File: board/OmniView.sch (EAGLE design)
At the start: 50 parts, among them Q1 CMA-4544PF-W, Q2 BSS138, Q3 BSS138, U1 SN74LVC2T45DCUT, U2 UG-2864HSWEG01

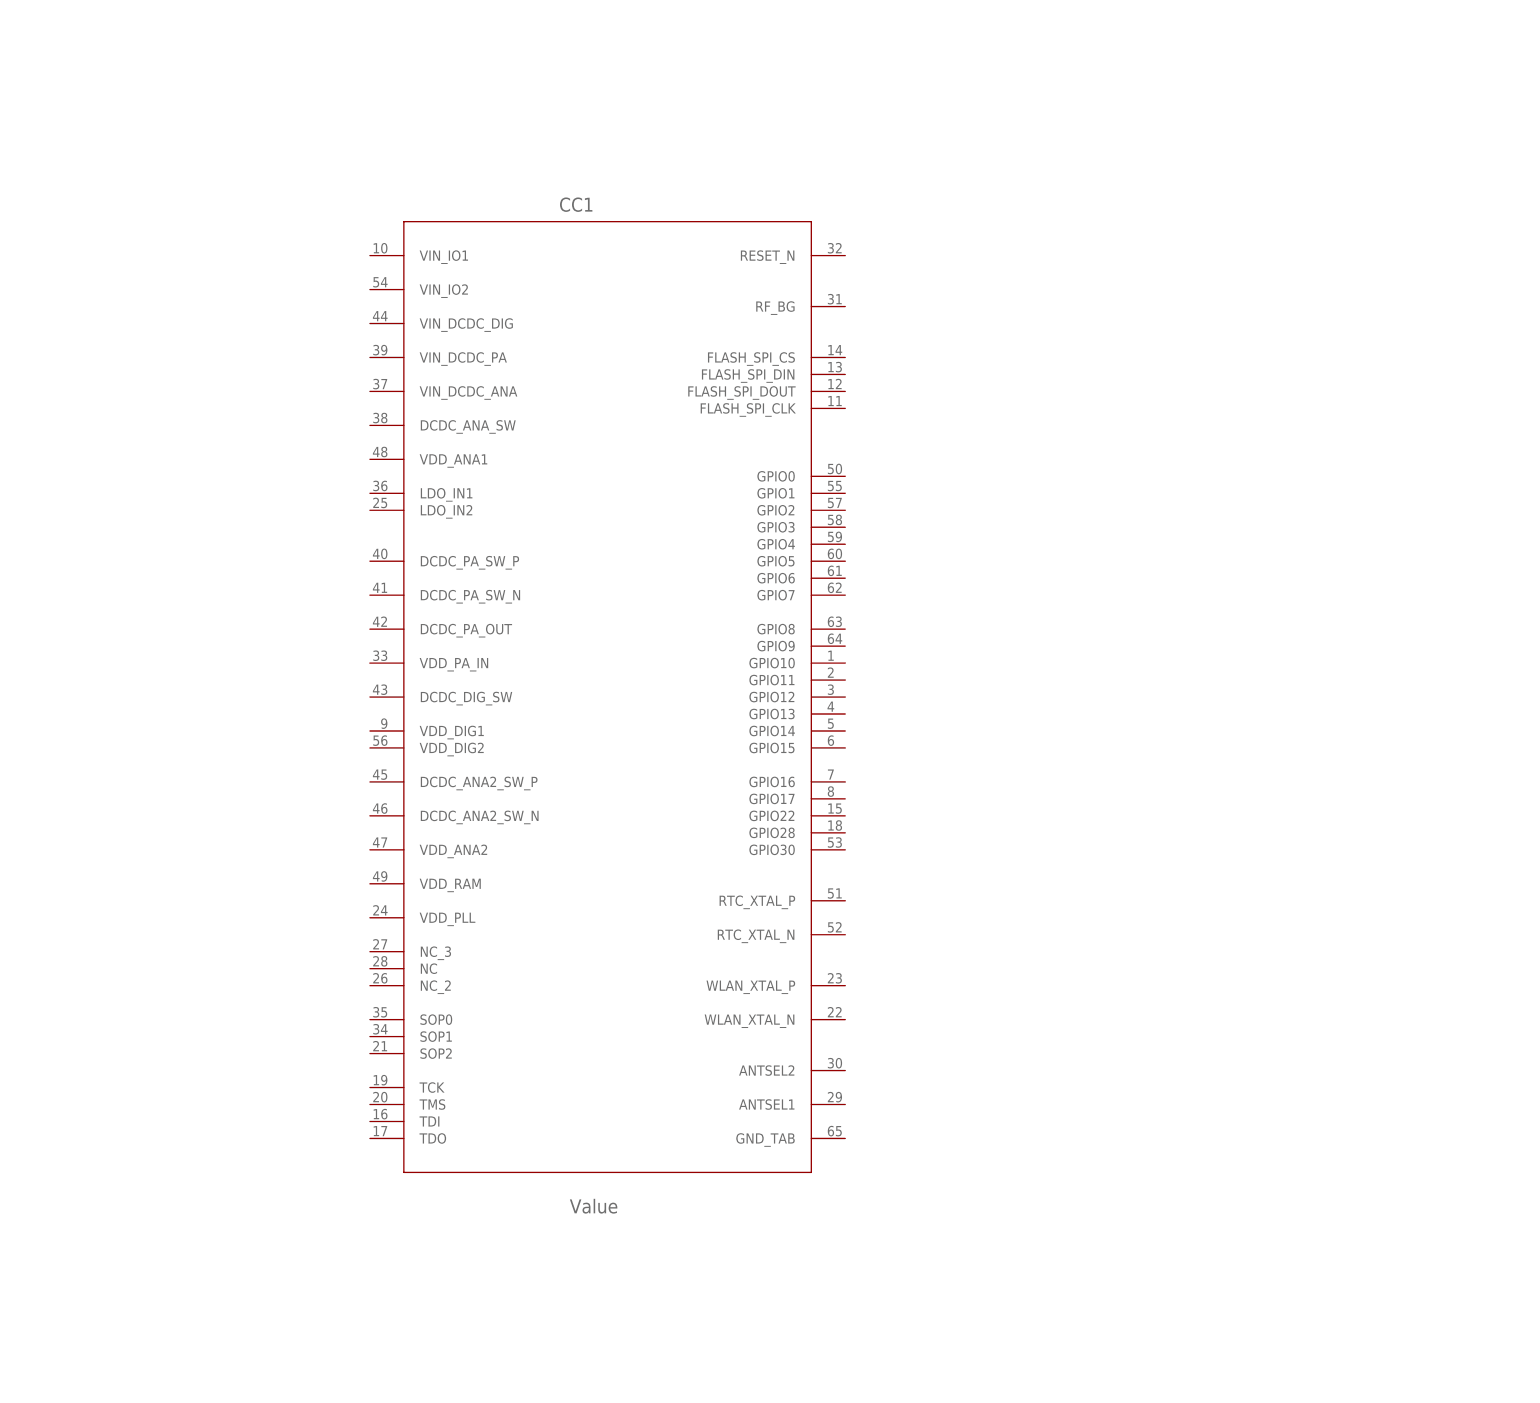
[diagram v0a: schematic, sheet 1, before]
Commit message: schematic check-up
did a little bit of schematic setting up
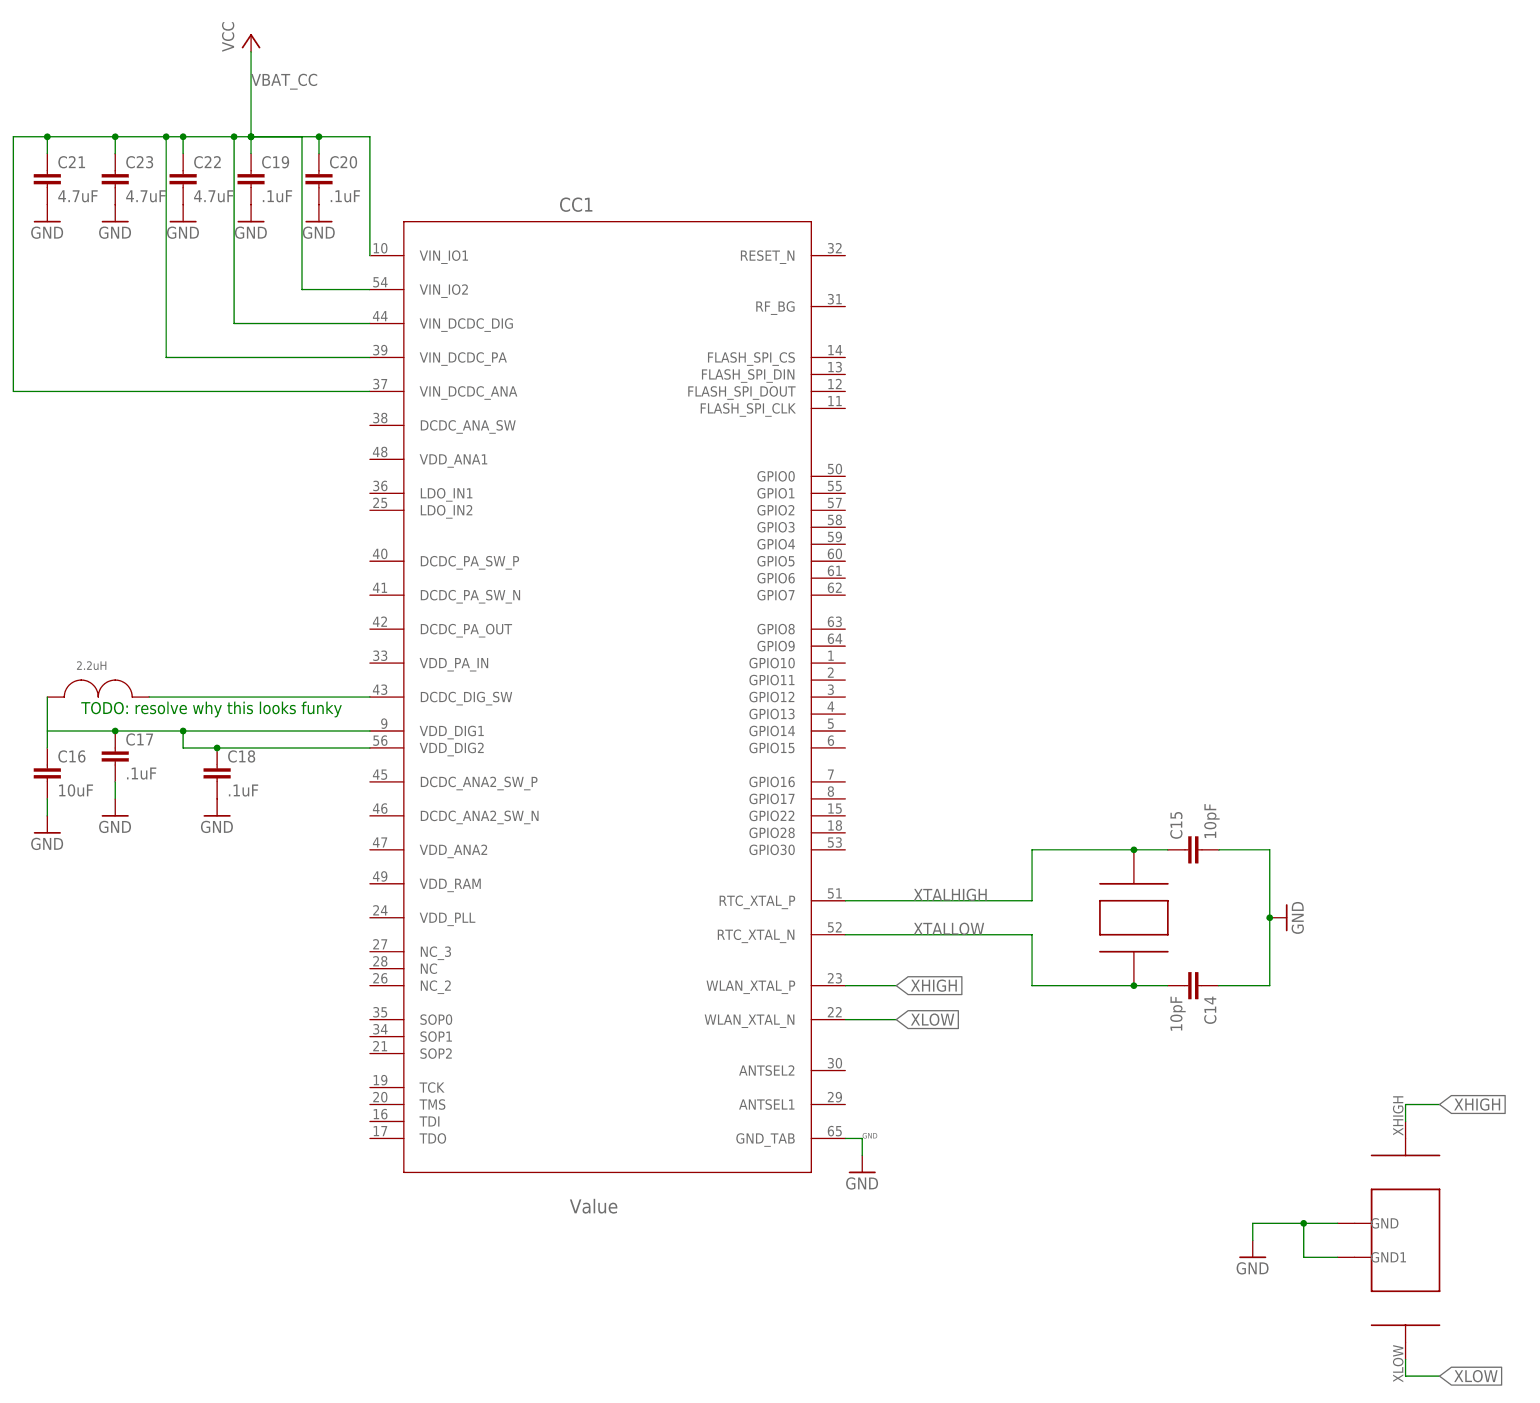
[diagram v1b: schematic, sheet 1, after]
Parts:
- added 32KHZ: ABS07, ABS07_crys:ABS07
- added C14, C15: 10pF, rcl:C-EUC0603
- added C16: 10uF, rcl:C-EUC0603
- added C17, C18, C19, C20: .1uF, rcl:C-EUC0603
- added C21, C22, C23: 4.7uF, rcl:C-EUC0603
- added U$27: 2.2uH, ABS07_crys:1008INDUCTOR
- added U$4: Q24FA20H00396, ABS07_crys:Q24FA20H00396
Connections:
- new net N$18: CC1.DCDC_DIG_SW, U$27.P$2
- new net N$19: C16.1, U$27.P$1
- new net N$20: C17.1, C18.1, CC1.VDD_DIG1, CC1.VDD_DIG2
- new net VBAT_CC: C19.1, C20.1, C21.1, C22.1, C23.1, CC1.VIN_DCDC_ANA, CC1.VIN_DCDC_DIG, CC1.VIN_DCDC_PA, CC1.VIN_IO1, CC1.VIN_IO2
- new net XHIGH: CC1.WLAN_XTAL_P, U$4.XHIGH
- new net XLOW: CC1.WLAN_XTAL_N, U$4.XLOW
- new net XTALHIGH: 32KHZ.XLOW, C15.1, CC1.RTC_XTAL_P
- new net XTALLOW: 32KHZ.XHIGH, C14.2, CC1.RTC_XTAL_N
- net GND: now also C14.1, C15.2, C16.2, C17.2, C18.2, C19.2, C20.2, C21.2, C22.2, C23.2, CC1.GND_TAB, U$4.GND, U$4.GND1
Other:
- note added: "TODO: resolve why this looks funky"

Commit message: schematic check-up
initial schematic done, beginning routing
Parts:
- removed 32KHZ: ABS07, ABS07_crys:ABS07
- removed C10, C3, C4: 10uF, microbuilder:CAP_CERAMIC0805
- removed C11, C13, C6, C7: 1uF, microbuilder:CAP_CERAMIC0805
- removed C12: 2.2uF/16V, microbuilder:CAP_CERAMIC0805
- removed C14, C15: 10pF, rcl:C-EUC0603
- removed C16: 10uF, rcl:C-EUC0603
- removed C17, C18, C19, C20: .1uF, rcl:C-EUC0603
- removed C21: 4.7uF, rcl:C-EUC0603
- removed CC1: Value, CC3200:CC3200R1M2RGCR
- removed D1, D2, D3: 1N4148, microbuilder:DIODESOD-323
- removed FID1, FID2: FIDUCIAL"", microbuilder:FIDUCIAL""
- removed IC1: (no value), ftdichip-3:FT2232D
- removed J2: (no value), microbuilder:HEADER-1X576MIL
- removed Q2, Q3: BSS138, microbuilder:MOSFET-NWIDE
- removed R14, R4: 10K, microbuilder:RESISTOR0805
- removed R8: 390K, microbuilder:RESISTOR0805
- removed SJ1, SJ2: (no value), microbuilder:SOLDERJUMPERREFLOW_NOPASTE
- removed SV1: (no value), con-lsta:FE10-2
- removed U$23, U$24, U$25, U$26: MOUNTINGHOLE2.5, microbuilder:MOUNTINGHOLE2.5
- removed U$27: 2.2uH, ABS07_crys:1008INDUCTOR
- removed U$4: Q24FA20H00396, ABS07_crys:Q24FA20H00396
- removed U2: UG-2864HSWEG01, microbuilder:DISP_OLED_UG-2864HSWEG010.96"
- removed U3: (no value), microbuilder:VREG_SOT23-5
- added ANT_PAD: ANT, Antenna:ANT
- added C24: .01uF, rcl:C-EUC0603
- added C25, C27: 10uF, rcl:C-EUC0603
- added C26: 15pF, rcl:C-EUC0603
- added C33: 1pF, rcl:C-USC0402
- added CC3200MOD: CC3200, cc3200mod:CC3200
- added JP3: (no value), pinhead:PINHD-1X7
- added JP6: (no value), pinhead:PINHD-2X10/90
- added L1: 3.6nH, Spark:INDUCTOR-SPARKFUN0402
- added R10, R9: 33, rcl:R-US_R0603
- added R16: 2.7K, SparkFun-Resistors:RESISTOR0603
- added R26: 10k, adafruit:R-US_R0805
- added R31: 52.3K, resistor:R-US_R0805
- added R32: 30.1K, resistor:R-US_R0805
- added R33: 0, SparkFun-Resistors:RESISTOR0603
- added R37, R41: 0, adafruit:R-US_R0805
- added SOP0, SOP2: (no value), pinhead:PINHD-1X2
- added U$30: TPS737_DCQ, tps737DCQ:TPS737_DCQ
- added U6: TPS79328DBVRG4, Texas Instruments_By_element14_Batch_1:TPS79328DBVRG4
- added X1, X2: FH12-24S-0.5SH, con-hirose:FH12-24S-0.5SH
- C22: value 4.7uF -> 2.2uF
- C23: value 4.7uF -> .1uF
- JP1: device microbuilder:HEADER-1X870MIL -> SparkFun-Connectors:M02-JST-2MM-SMT
- R1, R3: device adafruit:R-US_R0805 -> rcl:R-US_R0603
- R11, R12, R13: device microbuilder:RESISTOR0805 -> rcl:R-US_R0603
- R2: value 100k -> 100K; device adafruit:R-US_R0805 -> rcl:R-US_R0603
- R5: value 10K -> 2.7K; device microbuilder:RESISTOR0805 -> SparkFun-Resistors:RESISTOR0603
- R6, R7: value 10K -> 3.3K; device microbuilder:RESISTOR0805 -> rcl:R-US_R0603
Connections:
- removed net 3.3V: C11.P$2, C13.P$2, C4.P$1, JP1.6, Q2.G, Q3.G, R11.2, R12.2, R5.2, R6.2, R7.2, SJ2.1, U2.VBAT, U2.VDD, U3.OUT
- removed net A/R: J2.5, U$1.A/R
- removed net CS_3.3V: D1.A, R5.1, U2./CS
- removed net CS_5.0V: D1.C, JP1.5
- removed net D0/SCLK/SCK_3.3V: Q3.S, R12.1, U2.D0/SPI_SCLK/I2C_SCK
- removed net D0/SCLK/SCK_5.0V: JP1.2, Q3.D, R14.1
- removed net D1/MOSI/SDA1_3.3V: Q2.S, R11.1, SJ1.1, U2.D1/SPI_SDIN/I2C_SDA
- removed net D1/MOSI/SDA_5.0V: JP1.1, Q2.D, R13.1
- removed net DC/SA0_3.3V: D3.A, R7.1, U2.DC/I2C_SA0
- removed net DC/SA0_5.0V: D3.C, JP1.3
- removed net GAIN: J2.3, U$1.GAIN
- removed net N$2: FB1.P$1, J2.2
- removed net OUTPUT: J2.4, U$1.MICOUT
- removed net RST_3.3V: D2.A, R6.1, U2./RES
- removed net RST_5.0V: D2.C, JP1.4
- removed net VBAT_CC: C19.1, C20.1, C21.1, C22.1, C23.1, CC1.VIN_DCDC_ANA, CC1.VIN_DCDC_DIG, CC1.VIN_DCDC_PA, CC1.VIN_IO1, CC1.VIN_IO2
- removed net VDD: C1.1, FB1.P$2, U$1./SHDN, U$1.VDD
- removed net VIN: C3.P$1, JP1.7, R13.2, R14.2, U3.EN, U3.IN
- removed net XHIGH: CC1.WLAN_XTAL_P, U$4.XHIGH
- removed net XLOW: CC1.WLAN_XTAL_N, U$4.XLOW
- removed net XTALHIGH: 32KHZ.XLOW, C15.1, CC1.RTC_XTAL_P
- removed net XTALLOW: 32KHZ.XHIGH, C14.2, CC1.RTC_XTAL_N
- new net EN: JP6.17, R26.2, R9.1
- new net GPIO_01/PCK/FLASH_RX: CC3200MOD.46_GPIO1, JP3.5, JP6.8
- new net GPIO_03/D5: CC3200MOD.48_GPIO3, JP6.14
- new net GPIO_04/D4: CC3200MOD.49_GPIO4, JP6.13
- new net GPIO_05/D3: CC3200MOD.50_GPIO5, JP6.16
- new net GPIO_06/D2: CC3200MOD.51_GPIO6, JP6.15
- new net GPIO_07/OLED_RST: CC3200MOD.52_GPIO7
- new net GPIO_09/EN: CC3200MOD.54_GPIO9, R13.2, U1.A2
- new net GPIO_11/MCK: CC3200MOD.4_GPIO11, R12.2, U1.A1
- new net GPIO_12/VS: CC3200MOD.9_GPIO12, JP6.6
- new net GPIO_13/PHS: CC3200MOD.10_GPIO13, JP6.5
- new net GPIO_14/D6: CC3200MOD.5_GPIO14, JP6.11
- new net GPIO_15/D7: CC3200MOD.6_GPIO15, JP6.12
- new net GPIO_16/D8: CC3200MOD.7_GPIO16, JP6.9
- new net GPIO_17/D9: CC3200MOD.8_GPIO17, JP6.10
- new net GSPI_CS: CC3200MOD.44_GPIO0
- new net GSPI_MISO: CC3200MOD.42_GPIO30
- new net I2C_SCL: JP6.4, R41.2, R7.1
- new net I2C_SCL/JTAG_TDI: CC3200MOD.12JTAG_TDI, JP3.4, R41.1
- new net I2C_SDA: JP6.3, R37.2, R6.1
- new net I2C_SDA/JTAG_TDO: CC3200MOD.18_JTAG_TDO, JP3.3, R37.1
- new net JTAG_TCK: JP3.2
- new net JTAG_TMS: JP3.1
- new net LDO_2.8V: C22.2, R6.2, R7.2, U1.VCCB
- new net MCK: JP6.7, R10.1
- new net MICA/R: U$1.A/R
- new net MICGAIN: U$1.GAIN
- new net MICOUT: U$1.MICOUT
- new net MICOUT/FLASH_TX: CC3200MOD.47_GPO2, JP3.6
- new net MIC_VDD: FB1.P$1, U$1./SHDN, U$1.VDD
- new net N$21: ANT_PAD.FEED, C33.1, L1.1
- new net N$22: X1-17.1
- new net N$23: X1-18.1
- new net N$24: X1-19.1
- new net N$25: X1-20.1
- new net N$26: X1-21.1
- new net N$27: X1-22.1
- new net N$28: X1-23.1
- new net N$29: JP6.20
- new net N$30: X1-24.1
- new net N$31: X1-14.1
- new net N$32: X1-13.1
- new net N$33: X1-12.1
- new net N$34: X1-11.1
- new net N$35: X2-14.1
- new net N$36: X1-10.1
- new net N$37: X1-9.1
- new net N$38: X1-8.1
- new net N$39: X1-7.1
- new net N$40: JP6.19
- new net N$41: X1-6.1
- new net N$42: X1-5.1
- new net N$43: X1-4.1
- new net N$44: X1-3.1
- new net N$45: X1-2.1
- new net N$46: X1-1.1
- new net N$47: CC3200MOD.45_NC
- new net N$48: X2-13.1
- new net N$49: C22.1, U6.OUT
- new net N$50: R11.1, U1.DIR
- new net N$51: C24.1, U6.NR
- new net N$52: X2-12.1
- new net N$53: R10.2, U1.B1
- new net N$54: R9.2, U1.B2
- new net N$55: X2-11.1
- new net N$56: X2-10.1
- new net N$57: X2-9.1
- new net N$58: X2-8.1
- new net N$59: X2-7.1
- new net N$60: X2-6.1
- new net N$61: X2-5.1
- new net N$62: X2-4.1
- new net N$63: X2-3.1
- new net N$64: X2-2.1
- new net N$65: X2-1.1
- new net N$76: CC3200MOD.53_GPIO8
- new net N_RESET: CC3200MOD.35_N_RESET, JP3.7
- new net REGFB: R31.1, R32.2, U$30.NR/FB
- new net REGVOUT: C26.1, R31.2, R33.1, U$30.VOUT
- new net SOP0: CC3200MOD.34_SOP0, R5.1, SOP0.1
- new net SOP2: CC3200MOD.23_SOP2, R16.1, SOP2.1
- new net VBATT: C25.1, JP1.2, U$30.EN, U$30.VIN
- new net VCC: C1.1, C23.1, C27.1, CC3200MOD.36_VBAT_DCDC_ANA, CC3200MOD.37_VBAT_DCDC_PA, CC3200MOD.39_VDD_ANA2, CC3200MOD.40_VBAT_DCDC_DIG_IO, FB1.P$2, JP6.2, R11.2, R33.2, SOP0.2, SOP2.2, U1.VCCA, U6.EN, U6.IN
- net GND: now also ANT_PAD.GND4, ANT_PAD.GND5, C24.2, C25.2, C26.2, C27.2, C33.2, CC3200MOD.16_GND, CC3200MOD.1_GND, CC3200MOD.27_GND, CC3200MOD.28_GND, CC3200MOD.2_GND, CC3200MOD.30_GND, CC3200MOD.32_GND, CC3200MOD.38_GND, CC3200MOD.43_GND, CC3200MOD.55, CC3200MOD.56, CC3200MOD.57, CC3200MOD.58, CC3200MOD.59_GND, CC3200MOD.60_GND, CC3200MOD.61_GND, CC3200MOD.62_GND, CC3200MOD.63_GND, FB2.P$1, JP1.1, JP6.1, JP6.18, R12.1, R13.1, R16.2, R26.1, R32.1, R5.2, U$30.GND, U$30.TAB, U1.GND, U6.GND; no longer C10.P$1, C11.P$1, C12.P$1, C13.P$1, C14.1, C15.2, C16.2, C17.2, C18.2, C19.2, C20.2, C21.2, C22.2, C3.P$2, C4.P$2, CC1.GND_TAB, JP1.8, R4.1, R8.1, U$4.GND, U$4.GND1, U2.BS0, U2.BS2, U2.NC(GND)@1, U2.NC(GND)@2, U2.VLSS, U2.VSS, U3.GND
- net N$1: now also X2-15.1; no longer R4.2, SJ2.2, U2.BS1
- net N$10: now also R1.2; no longer R1.1
- net N$11: now also R1.1; no longer R1.2
- net N$12: now also X2-19.1; no longer C6.P$1, U2.C2N
- net N$13: now also X2-20.1; no longer C7.P$2, U2.C1P
- net N$14: now also X2-21.1; no longer C7.P$1, U2.C1N
- net N$15: now also X2-22.1; no longer C10.P$2, U2.VCC
- net N$16: now also X2-23.1; no longer C12.P$2, U2.VCOMH
- net N$17: now also X2-24.1; no longer SJ1.2, U2.D2/I2C_SDA
- net N$18: now also X1-15.1; no longer CC1.DCDC_DIG_SW, U$27.P$2
- net N$19: now also CC3200MOD.31_RF_BG, L1.2; no longer C16.1, U$27.P$1
- net N$20: now also X1-16.1; no longer C17.1, C18.1, CC1.VDD_DIG1, CC1.VDD_DIG2
- net N$3: now also X2-16.1; no longer FB2.P$1, J2.1
- net N$4: now also X2-17.1; no longer R8.2, U2.IREF
- net N$6: now also X2-18.1; no longer C6.P$2, U2.C2P
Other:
- note added: "Antenna"
- note added: "Attack/Release ratio is 1:4000 while floating"
- note added: "Gain is 60dB while floating"
- note added: "Logic Shifter"
- note added: "MCU I/O"
- note added: "MIC"
- note added: "Ribbon Cable"
- note added: "TODO: add battery connector"
- note added: "TODO: verify that the resistor needs to be there"
- note added: "what if the camera breakout takes care of this?"
- note removed: "Bus default = SPI4"
- note removed: "Close SJ2 for I2C"
- note removed: "Close for"
- note removed: "I think this guy is the same as SN74LVC2T45DCTR.They have the same datasheet"
- note removed: "I2C"
- note removed: "TODO: resolve why this looks funky"

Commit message: initial board push
first revision of board is...done! This revision still needs to:
-review antenna trace with expert
-clean up some of the routing
-be reviewed by non-john member of the team
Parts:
- removed C1, C5: 2.2uF, adafruit:C-USC0805K
- removed C2, C9: 0.1uF, adafruit:C-USC0805K
- removed C8: 0.47uF, adafruit:C-USC0805K
- removed FB1, FB2: FERRITE, microbuilder:FERRITE0805
- removed JP6: (no value), pinhead:PINHD-2X10/90
- removed Q1: CMA-4544PF-W, adafruit:ELECTRET
- removed R2: 100K, rcl:R-US_R0603
- removed R26: 10k, adafruit:R-US_R0805
- removed R3: 2.2K, rcl:R-US_R0603
- removed R33: 0, SparkFun-Resistors:RESISTOR0603
- removed R37, R41: 0, adafruit:R-US_R0805
- removed U$1: MAX9814TDFN14, adafruit:MAX9814TDFN14
- removed X1, X2: FH12-24S-0.5SH, con-hirose:FH12-24S-0.5SH
- added R4: 100k, SparkFun-Resistors:RESISTOR0603
- added SV1: (no value), con-dil:16P
- R1: value 150k -> 10k; device rcl:R-US_R0603 -> resistor:R-US_R0603
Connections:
- net N$19 renamed MCU_RF
- removed net I2C_SCL: JP6.4, R41.2, R7.1
- removed net I2C_SDA: JP6.3, R37.2, R6.1
- removed net INPUT: C9.2, Q1.2, R3.1
- removed net MICA/R: U$1.A/R
- removed net MICGAIN: U$1.GAIN
- removed net MICOUT: U$1.MICOUT
- removed net MIC_VDD: FB1.P$1, U$1./SHDN, U$1.VDD
- removed net N$1: X2-15.1
- removed net N$10: R1.2, R2.2, U$1.TH
- removed net N$11: R1.1, R3.2, U$1.MICBIAS
- removed net N$12: X2-19.1
- removed net N$13: X2-20.1
- removed net N$14: X2-21.1
- removed net N$15: X2-22.1
- removed net N$16: X2-23.1
- removed net N$17: X2-24.1
- removed net N$18: X1-15.1
- removed net N$20: X1-16.1
- removed net N$22: X1-17.1
- removed net N$23: X1-18.1
- removed net N$24: X1-19.1
- removed net N$25: X1-20.1
- removed net N$26: X1-21.1
- removed net N$27: X1-22.1
- removed net N$28: X1-23.1
- removed net N$29: JP6.20
- removed net N$3: X2-16.1
- removed net N$30: X1-24.1
- removed net N$31: X1-14.1
- removed net N$32: X1-13.1
- removed net N$33: X1-12.1
- removed net N$34: X1-11.1
- removed net N$35: X2-14.1
- removed net N$36: X1-10.1
- removed net N$37: X1-9.1
- removed net N$38: X1-8.1
- removed net N$39: X1-7.1
- removed net N$4: X2-17.1
- removed net N$40: JP6.19
- removed net N$41: X1-6.1
- removed net N$42: X1-5.1
- removed net N$43: X1-4.1
- removed net N$44: X1-3.1
- removed net N$45: X1-2.1
- removed net N$46: X1-1.1
- removed net N$48: X2-13.1
- removed net N$49: C22.1, U6.OUT
- removed net N$5: C9.1, U$1.MICIN
- removed net N$52: X2-12.1
- removed net N$55: X2-11.1
- removed net N$56: X2-10.1
- removed net N$57: X2-9.1
- removed net N$58: X2-8.1
- removed net N$59: X2-7.1
- removed net N$6: X2-18.1
- removed net N$60: X2-6.1
- removed net N$61: X2-5.1
- removed net N$62: X2-4.1
- removed net N$63: X2-3.1
- removed net N$64: X2-2.1
- removed net N$65: X2-1.1
- removed net N$7: C8.1, U$1.BIAS
- removed net N$8: C2.1, U$1.CT
- removed net N$9: C5.1, U$1.CG
- removed net REGVOUT: C26.1, R31.2, R33.1, U$30.VOUT
- net EN: now also R1.2, SV1.11; no longer JP6.17, R26.2
- net GND: now also C22.2, JP1.2, R1.1, R4.2; no longer C1.2, C2.2, C26.2, C5.2, C8.2, FB2.P$1, FB2.P$2, JP1.1, JP6.1, JP6.18, Q1.1, R2.1, R26.1, U$1.EP, U$1.GND, U$1.NC1, U$1.NC2
- net GPIO_01/PCK/FLASH_RX: now also SV1.2; no longer JP3.5, JP6.8
- net GPIO_03/D5: now also SV1.3; no longer JP6.14
- net GPIO_04/D4: now also SV1.6; no longer JP6.13
- net GPIO_05/D3: now also SV1.5; no longer JP6.16
- net GPIO_06/D2: now also SV1.4; no longer JP6.15
- net GPIO_12/VS: now also SV1.14; no longer JP6.6
- net GPIO_13/PHS: now also SV1.13; no longer JP6.5
- net GPIO_14/D6: now also SV1.8; no longer JP6.11
- net GPIO_15/D7: now also SV1.7; no longer JP6.12
- net GPIO_16/D8: now also SV1.10; no longer JP6.9
- net GPIO_17/D9: now also SV1.9; no longer JP6.10
- net I2C_SCL/JTAG_TDI: now also R7.1, SV1.15; no longer R41.1
- net I2C_SDA/JTAG_TDO: now also R6.1, SV1.16; no longer R37.1
- net JTAG_TCK: now also CC3200MOD.21_JTAG_TCK
- net JTAG_TMS: now also CC3200MOD.22_JTAP_TMS, R4.1
- net LDO_2.8V: now also C22.1, U6.OUT; no longer C22.2
- net MCK: now also SV1.12; no longer JP6.7
- net MICOUT/FLASH_TX: now also JP3.5, SV1.1; no longer JP3.6
- net REGFB: now also C26.2
- net VBATT: now also JP1.1; no longer JP1.2
- net VCC: now also C26.1, R31.2, U$30.VOUT; no longer C1.1, FB1.P$2, JP6.2, R33.2
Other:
- note removed: "Attack/Release ratio is 1:4000 while floating"
- note removed: "Gain is 60dB while floating"
- note removed: "MCU I/O"
- note removed: "MIC"
